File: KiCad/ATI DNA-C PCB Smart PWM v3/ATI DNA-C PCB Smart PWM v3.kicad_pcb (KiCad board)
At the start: 2 copper layers, 70 x 20 mm, 18 parts, among them U1 SmartPWMv3

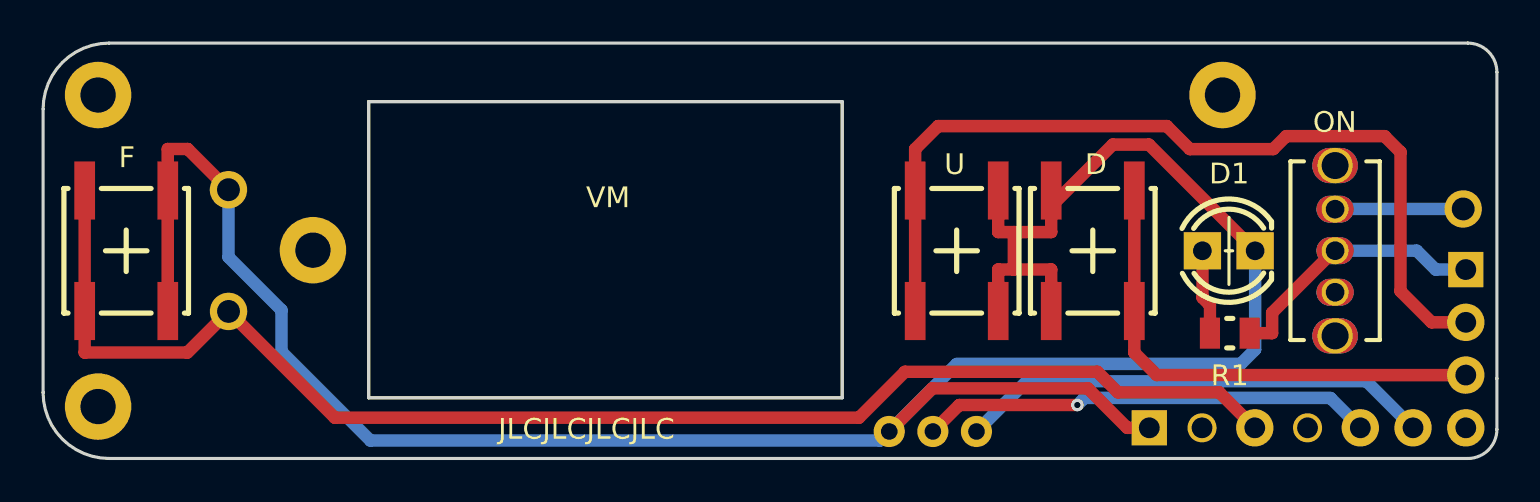
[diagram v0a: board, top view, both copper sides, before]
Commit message: Beef up pads, add MorningMist logo
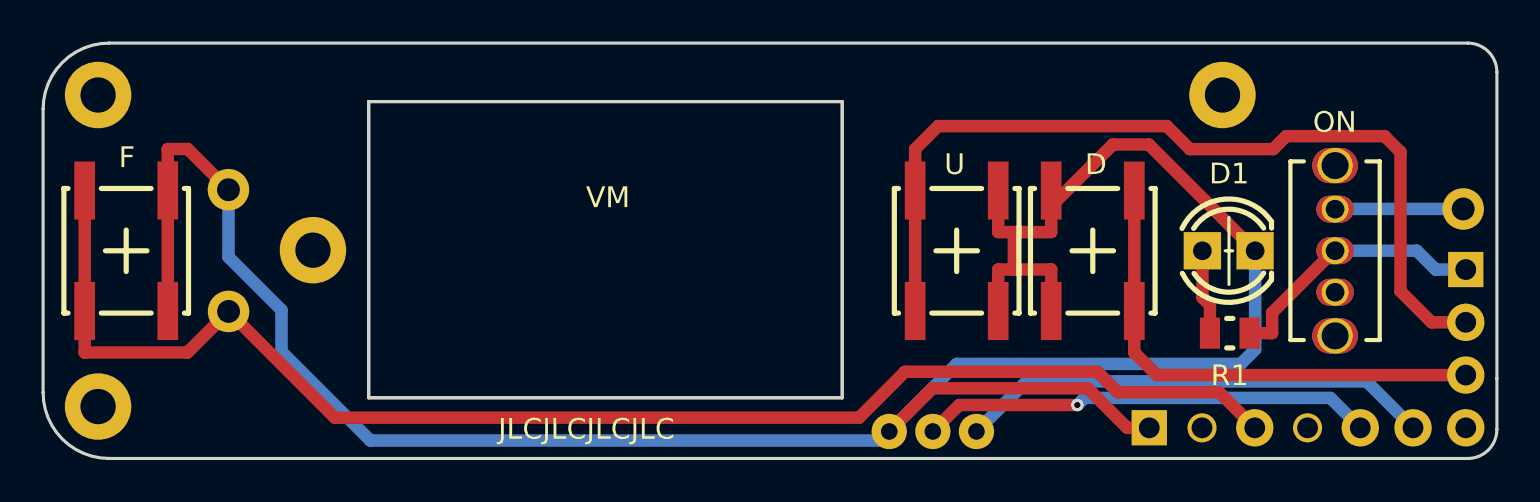
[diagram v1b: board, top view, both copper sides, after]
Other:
- board text added: "Powered by"
